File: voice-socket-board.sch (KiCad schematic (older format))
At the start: 258 parts

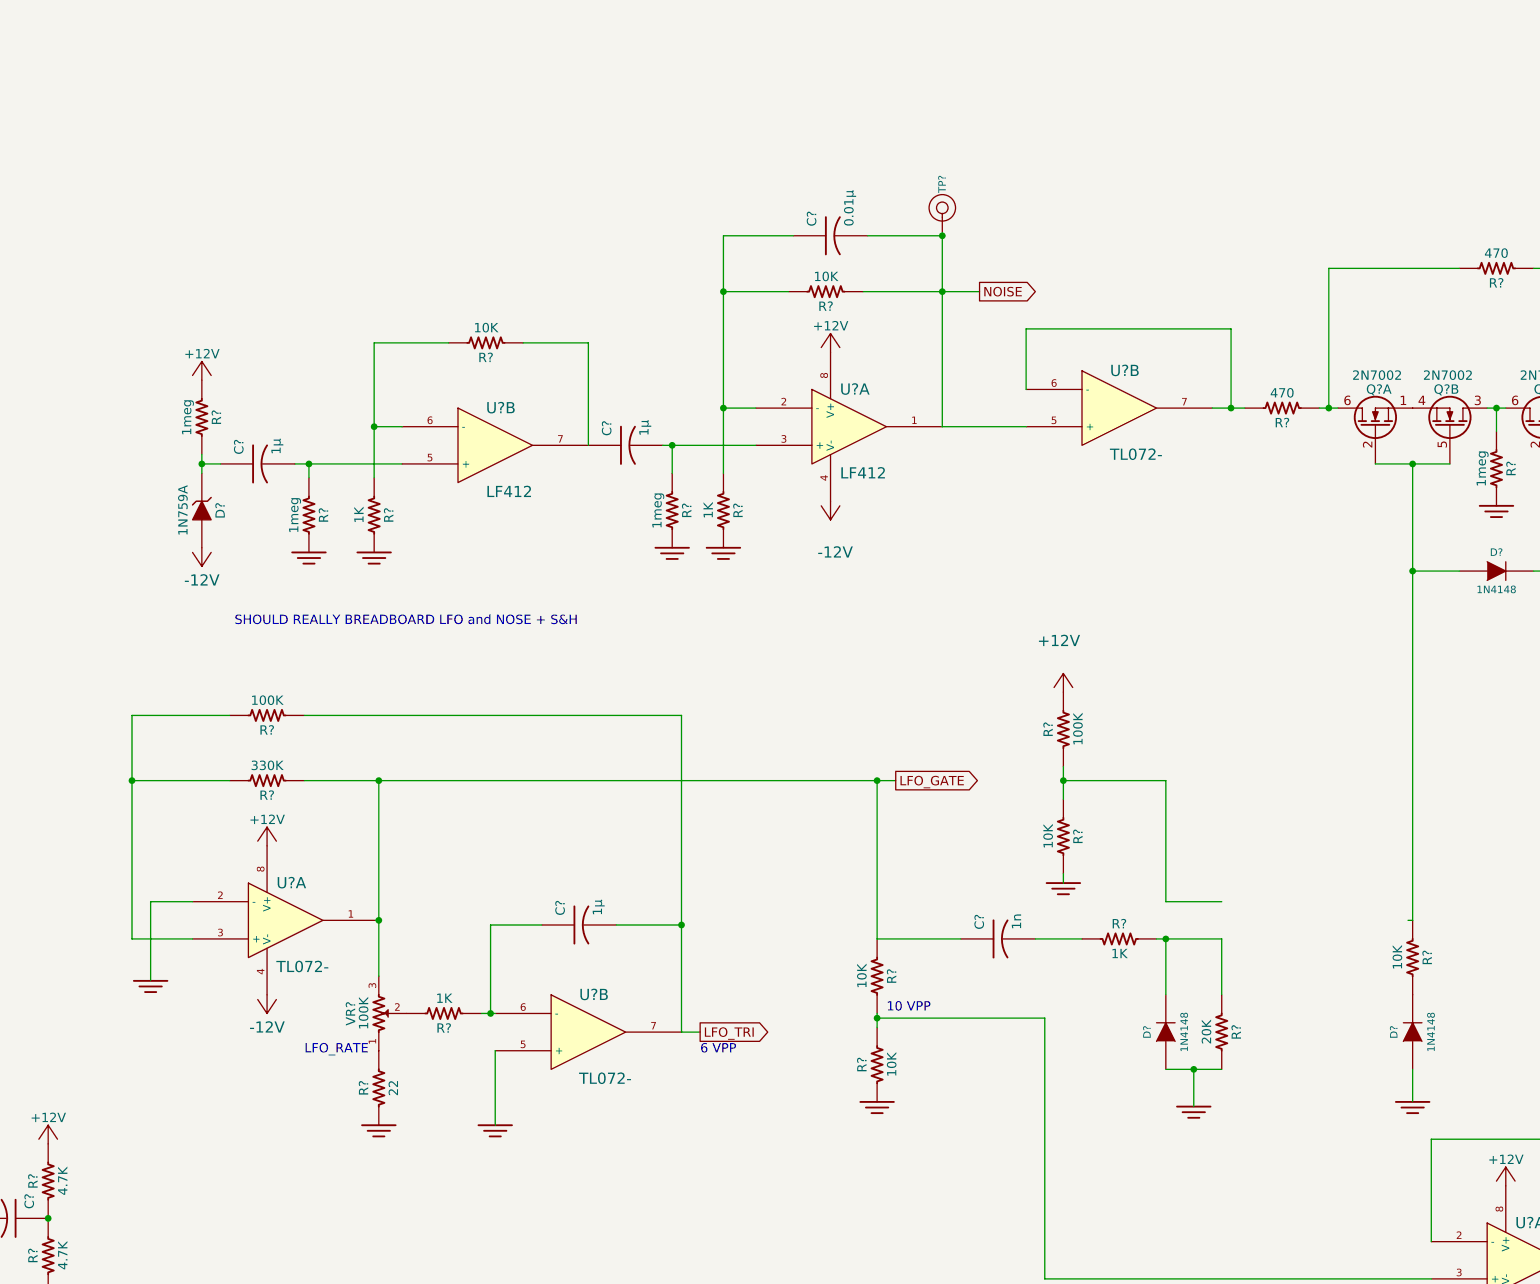
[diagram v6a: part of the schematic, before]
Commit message: changed noise source to an eeweb simple white noise generator. breadboarded EDN zener noise source and couldn't get it to work
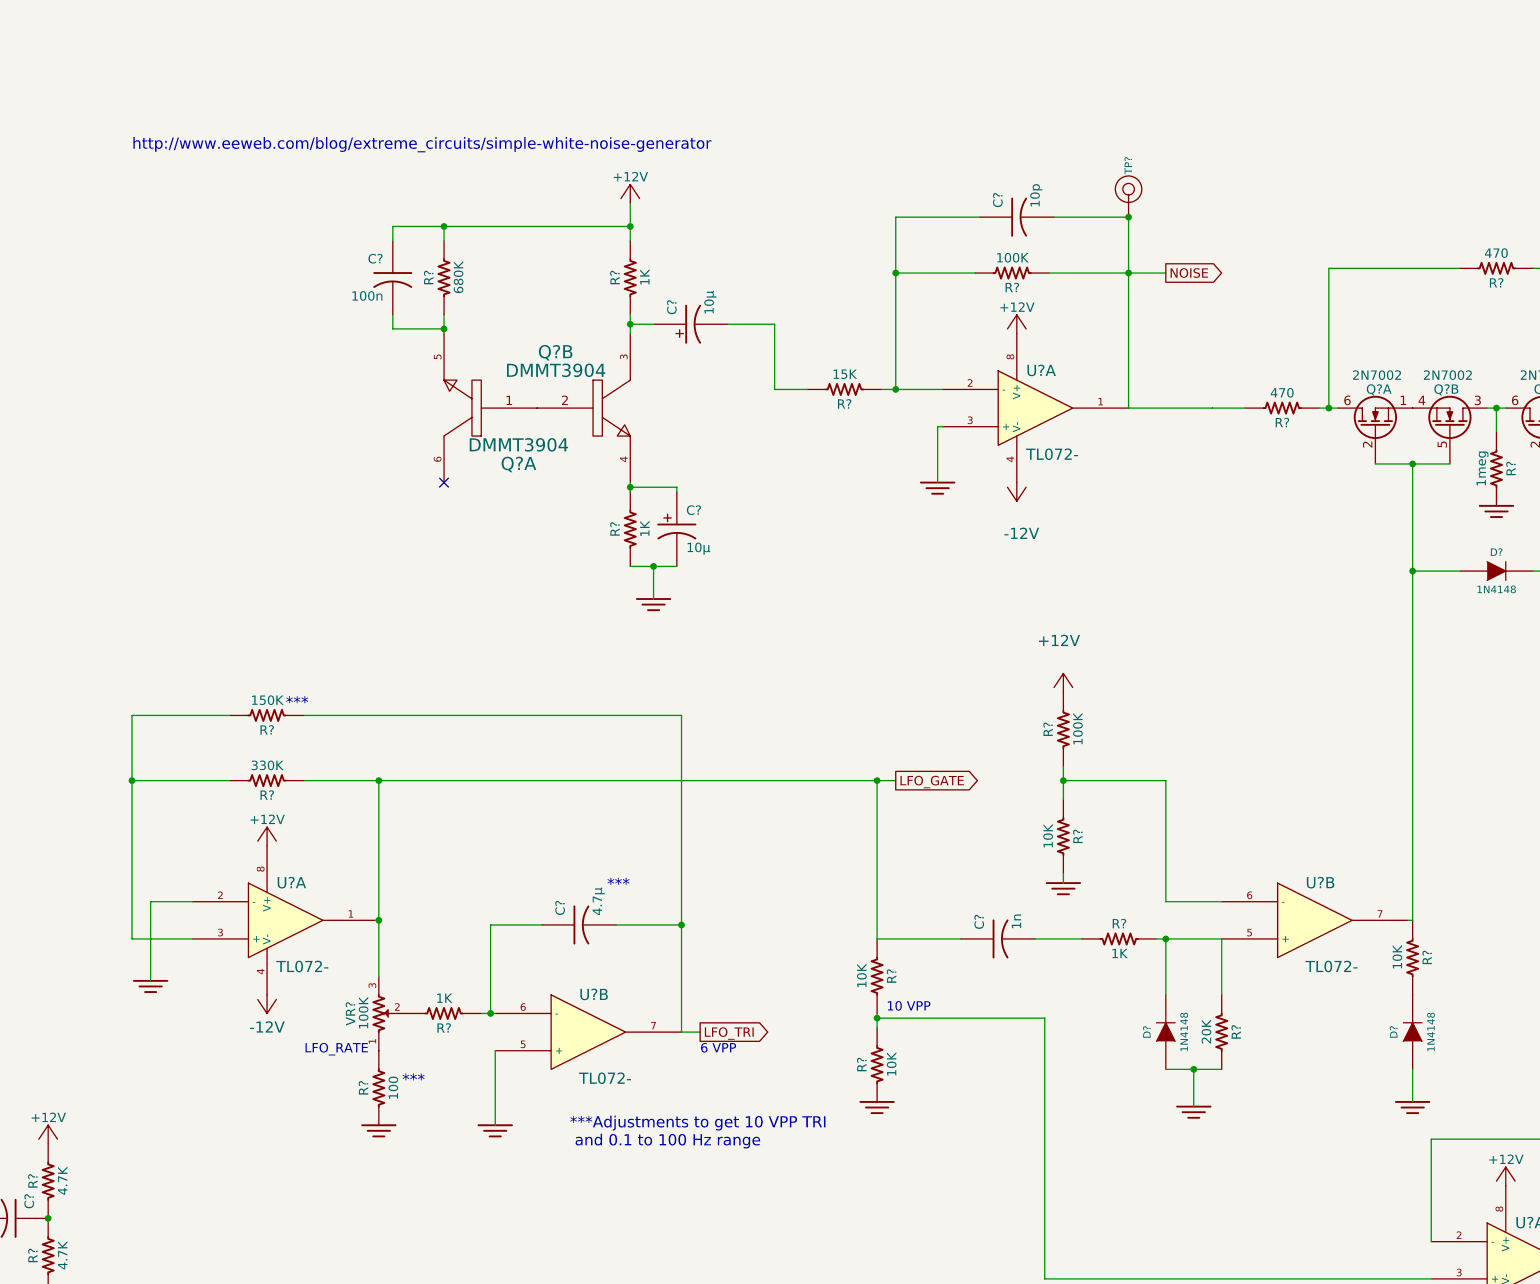
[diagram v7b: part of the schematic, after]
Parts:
- removed C? (x2): 1μ, symbol C_US
- removed D?: 1N759A, symbol ZENER
- removed R? (x3): 1meg, symbol R_US
- removed R? (x2): 1K, symbol R_US
- removed R?: 10K, symbol R_US
- removed U? (x2): LF412, ~, symbol TL072-
- removed U?: TL072-, symbol TL072-
- added C? (x2): 10μ, symbol CP_US
- added C?: 100n, symbol C_US
- added Q? (x2): DMMT3904, symbol DMMT3904
- added R? (x2): 1K, symbol R_US
- added R?: 680K, symbol R_US
- added R?: 15K, symbol R_US
- added U? (x2): TL072-, symbol TL072-
- C?: value 0.01μ -> 10p
- C?: value 1μ -> 4.7μ
- R?: value 10K -> 100K
- R?: value 100K -> 150K
- R?: value 22 -> 100
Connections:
- net +12V: now also C?.1, R?.2, R?.2, U?.8 (V+)
- net -12V: now also U?.4 (V-)
- net GND: now also C?.2 (-), R?.1, U?.3 (+)
- net NOISE: now also R?.2, U?.1
- net at R?.1, R?.1: now also U?.6 (-)
- net at D?.2 (K), R?.1, R?.2: now also U?.5 (+)
- net at C?.1, R?.2: now also R?.1, U?.2 (-)
- net at D?.1 (A), Q?.2 (G), Q?.5 (G)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: now also U?.7
- new net: Q?.1, Q?.2
- new net: C?.2, Q?.5, R?.1
- new net: C?.1 (+), Q?.3, R?.1
- new net: C?.1 (+), Q?.4, R?.2
- new net: C?.2 (-), R?.2
- no-connect marks 16 -> 17
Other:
- note added: "***"
- note added: "***Adjustments to get 10 VPP TRI\n and 0.1 to 100 Hz range"
- note added: "http://www.eeweb.com/blog/extreme_circuits/simple-white-noise-generator"
- note removed: "SHOULD REALLY BREADBOARD LFO and NOSE + S&H\n"
- moved on the sheet: C?, R?, TP?

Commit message: breadboarded noise, LFO and S&H. Changes based on testing added to schematic
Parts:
- removed D?: 1N4148, ~, symbol DIODE
- removed R?: 10K, symbol R_US
- added R?: 18K, symbol R_US
- added R?: 2.7K, symbol R_US
- added R?: 120K, symbol R_US
- R?: value 1K -> 4.7K
- R?: value 82K -> 47K
- R?: value 82K -> 100K
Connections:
- net +12V: now also R?.2; no longer C?.1
- net GND: now also C?.1, R?.2, R?.1, R?.1; no longer R?.1, U?.5 (+)
- net at C?.1 (+), Q?.4: now also R?.1; no longer R?.2
- net at D?.2 (K), Q?.2 (G), Q?.5 (G): now also R?.2
- net at C?.1, Q?.3 (D), U?.2 (-): no longer R?.1
- net at C?.2, R?.2, U?.6: now also R?.1
- new net: R?.1, R?.2, U?.5 (+)
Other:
- note added: "This offsets the 200 mV \nFET pedestal voltage"
- note added: "WHY IS THIS OP AMP FLIPPED OVER????"
- moved on the sheet: C?, Q?A, Q?B, R?
